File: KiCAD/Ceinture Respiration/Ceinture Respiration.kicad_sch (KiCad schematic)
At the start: 0 parts

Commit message: First draft PCB and sch
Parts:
- added A1: Arduino_Nano_v3.x, Module:Arduino_Nano, symbol MCU_Module:Arduino_Nano_v3.x
- added BT1: BH9VPC, CentureResp:BAT_BH9VPC, symbol CeintureRespAT:BH9VPC
- added C1, C2: 10uF, Capacitor_SMD:C_0603_1608Metric, symbol Device:C
- added D1, D2: DIODE, Diode_SMD:D_SOD-123, symbol pspice:DIODE
- added D3: LED, LED_THT:LED_D3.0mm, symbol Device:LED
- added D4: RED, LED_THT:LED_D3.0mm, symbol Device:LED
- added D5: ORANGE, LED_THT:LED_D3.0mm, symbol Device:LED
- added D6: GREEN, LED_THT:LED_D3.0mm, symbol Device:LED
- added D7: D_Schottky, Diode_SMD:D_SOD-123, symbol Device:D_Schottky
- added J1, J2: DIN-8, CentureResp:CUI_SDS-80J, symbol Connector:DIN-8
- added J3: Conn_01x04, Connector_PinSocket_2.54mm:PinSocket_1x04_P2.54mm_Vertical, symbol Connector_Generic:Conn_01x04
- added J4: MEM2061-01-188-00-A_REVA, CentureResp:GCT_MEM2061-01-188-00-A_REVA, symbol CeintureRespAT:MEM2061-01-188-00-A_REVA
- added J5: Conn_01x02, Buzzer_Beeper:Buzzer_Murata_PKMCS0909E, symbol Connector_Generic:Conn_01x02
- added J6: Conn_01x02, symbol Connector_Generic:Conn_01x02
- added J7: Conn_01x10_Pin, Connector_PinHeader_2.54mm:PinHeader_2x05_P2.54mm_Horizontal, symbol Connector:Conn_01x10_Pin
- added J8: Conn_01x10_Socket, Connector_PinSocket_2.54mm:PinSocket_2x05_P2.54mm_Horizontal, symbol Connector:Conn_01x10_Socket
- added PS1: RS3-0505D, CONV_RS3-0505D, symbol CeintureRespAT:RS3-0505D
- added Q1, Q2: MMBT3904, Package_TO_SOT_SMD:SOT-23, symbol Transistor_BJT:MMBT3904
- added R1, R10, R2, R3, R4, R5: 10K, Resistor_SMD:R_0603_1608Metric, symbol Device:R
- added R11, R6, R7, R8, R9: 1K, Resistor_SMD:R_0603_1608Metric, symbol Device:R
- added S1: EG1218, CentureResp:EG1218, symbol CeintureRespAT:EG1218
- added SW1, SW2, SW3, SW4: SW_Push, Button_Switch_SMD:SW_SPST_TL3305B, symbol Switch:SW_Push
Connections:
- new net: D4.2 (A), R7.1
- new net: Q2.1 (B), R2.2
- new net: Q1.1 (B), R1.2
- new net: D6.2 (A), R9.1
- new net: BT1.+, D7.2 (A)
- new net: D5.2 (A), R8.1
- new net: D7.1 (K), S1.S
- new net: J4.8 (DAT1), R5.2
- new net: J4.1 (DAT2), R4.2
- new net +3.3V: A1.17 (3V3), J3.2 (Pin_2), J4.4 (VDD), R3.1, R4.1, R5.1
- new net +5V: A1.27 (+5V), Q1.3 (C), Q2.3 (C)
- new net +5VA: J1.1, J2.1, PS1.6 (+VOUT), R6.2
- new net +BATT: J8.3 (Pin_3), PS1.2 (+VIN), S1.P
- new net -5VA: J1.4, J2.4, PS1.8 (-VOUT)
- new net A1: J7.1 (Pin_1)
- new net A2: J7.2 (Pin_2)
- new net BATT_VOLTAGE: A1.19 (A0), R10.2, R11.1
- new net BTN1: A1.25 (A6), SW2.1
- new net BTN2: A1.26 (A7), SW3.1
- new net BTN3: A1.11 (D8), SW1.1
- new net BTN4: A1.12 (D9), SW4.1
- new net BUZZER: A1.8 (D5), R1.1
- new net BUZZER_P: C1.1, D1.2 (A), J5.1 (Pin_1), Q1.2 (E)
- new net Belt_1: J1.3, J8.1 (Pin_1)
- new net Belt_2: J2.3, J8.2 (Pin_2)
- new net GND: A1.29 (GND), A1.4 (GND), C1.2, C2.2, D1.1 (K), D2.1 (K), D4.1 (K), D5.1 (K), D6.1 (K), J3.1 (Pin_1), J4.11 (GND), J4.12 (GND), J4.6 (VSS), J5.2 (Pin_2), J6.2 (Pin_2), J7.4 (Pin_4), R11.2, SW1.2, SW2.2, SW3.2, SW4.2
- new net GND1: BT1.-, D3.1 (K), J1.7, J2.7, J8.4 (Pin_4), PS1.1 (-VIN), PS1.3 (CTRL), PS1.7 (COM)
- new net LED1: A1.5 (D2), R7.2
- new net LED2: A1.6 (D3), R8.2
- new net LED3: A1.7 (D4), R9.2
- new net MISO: A1.15 (D12), J4.7 (DAT0)
- new net MOSI: A1.14 (D11), J4.3 (CMD)
- new net MOTOR: A1.9 (D6), R2.1
- new net MOTOR_P: C2.1, D2.2 (A), J6.1 (Pin_1), Q2.2 (E)
- new net PWR_LED: D3.2 (A), R6.1
- new net SCK: A1.16 (D13), J4.5 (CLK)
- new net SCL: A1.24 (A5), J3.3 (Pin_3)
- new net SDA: A1.23 (A4), J3.4 (Pin_4)
- new net SD_CS: A1.13 (D10), J4.2 (CD/DAT3), R3.2
- new net Signal_1: A1.20 (A1)
- new net Signal_2: A1.21 (A2)
- new net VDD: A1.30 (VIN), J7.3 (Pin_3), R10.1
- no-connect marks 0 -> 2
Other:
- removed sheet CONNECTOR
- removed sheet DEVICES
- removed sheet MCU
- removed sheet PSU
- note added: "BUZZER"
- note added: "DIN 8P -> SDS-80J"
- note added: "GOGOSSE Switch-1/0 2X BTN Vibration Buzzer LED PWR LED Indicator RGB SD card"
- note added: "I2C Screen"
- note added: "INPUT RANGE 4.5V-9V"
- note added: "MCU NANO PINOUT ARDUINO NANO BLE 33"
- note added: "RS3-0505D avec une batterie 9V"
- note added: "Référence https://content.arduino.cc/assets/NANO33BLE_V4.0_sch.pdf?_gl=1*1v2d5tn*_ga*MTgwOTc4MjI5MC4xNjg2OTY2OTQz*_ga_NEXN8H46L5*MTY4Njk3MDgyNi4yLjEuMTY4Njk3MTE2NC4wLjAuMA.."
- note added: "VIB"
- note added: "connector for sensor DIN"
- note removed: "AUTRE GOGOSSE Switch-1/0 2X BTN Vibration Buzzer LED PWR LED Indicator RGB SD card"
- note removed: "Connector USB-C - programming connector for sensor DIN JST PH li-po"
- note removed: "MCU Feather datalogger ..."
- note removed: "PSU +/- 12V Li-Po USB Charge"

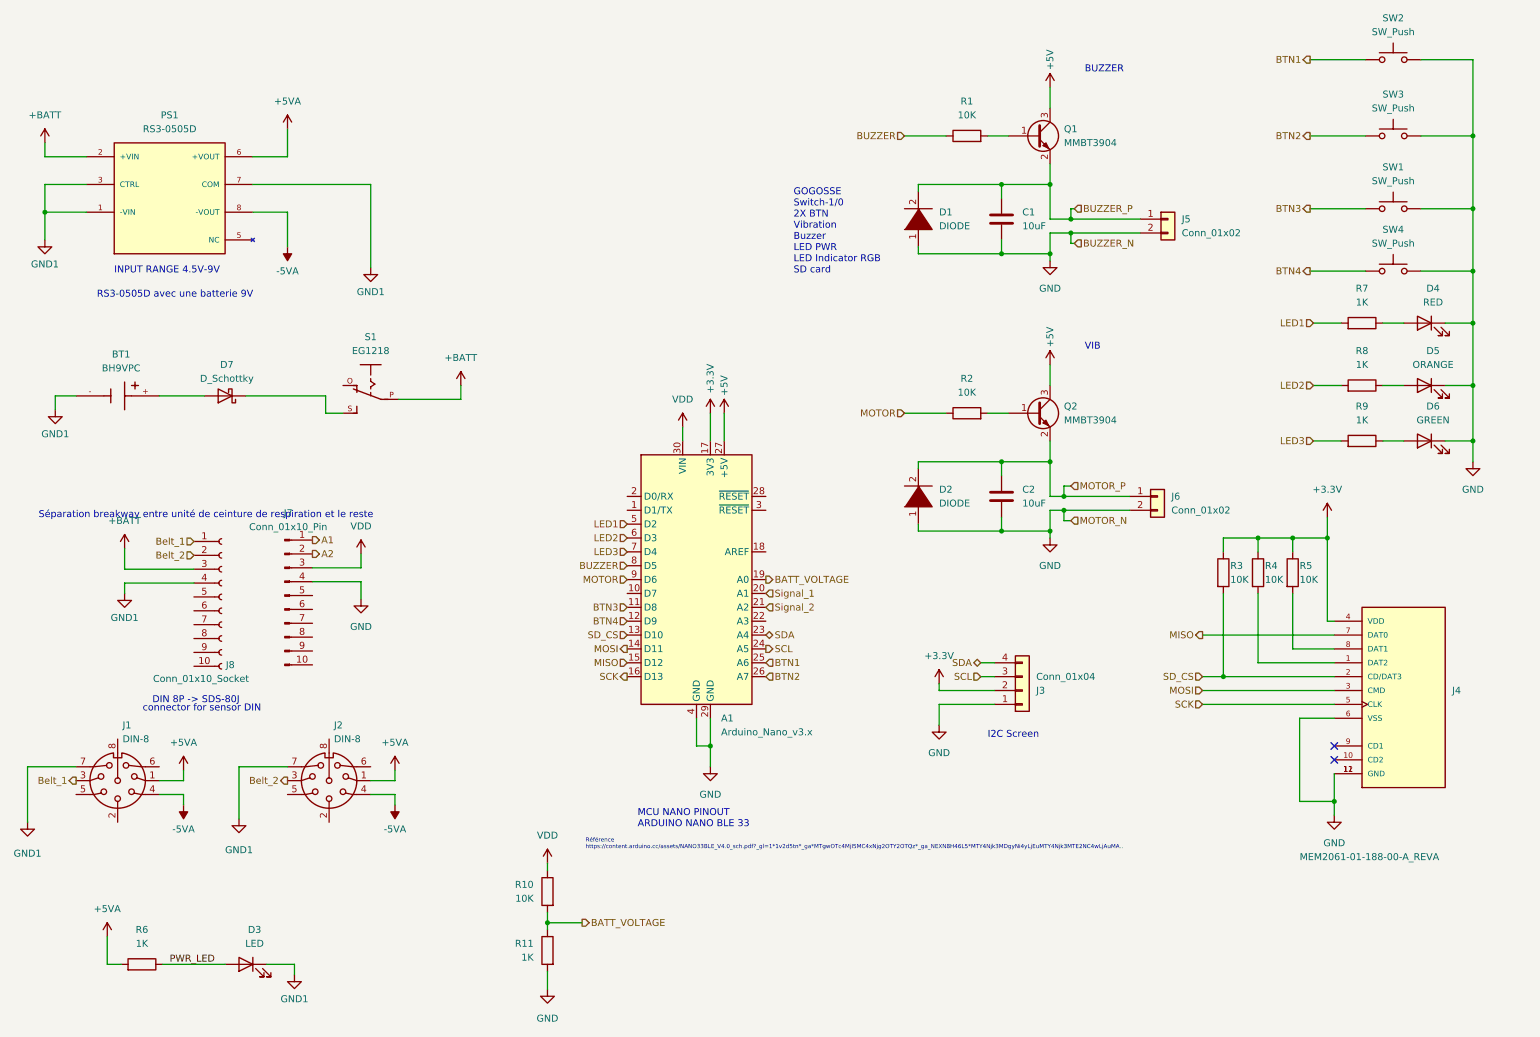
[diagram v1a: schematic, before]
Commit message: Scématique complété
Reste quelques footprint à configurer
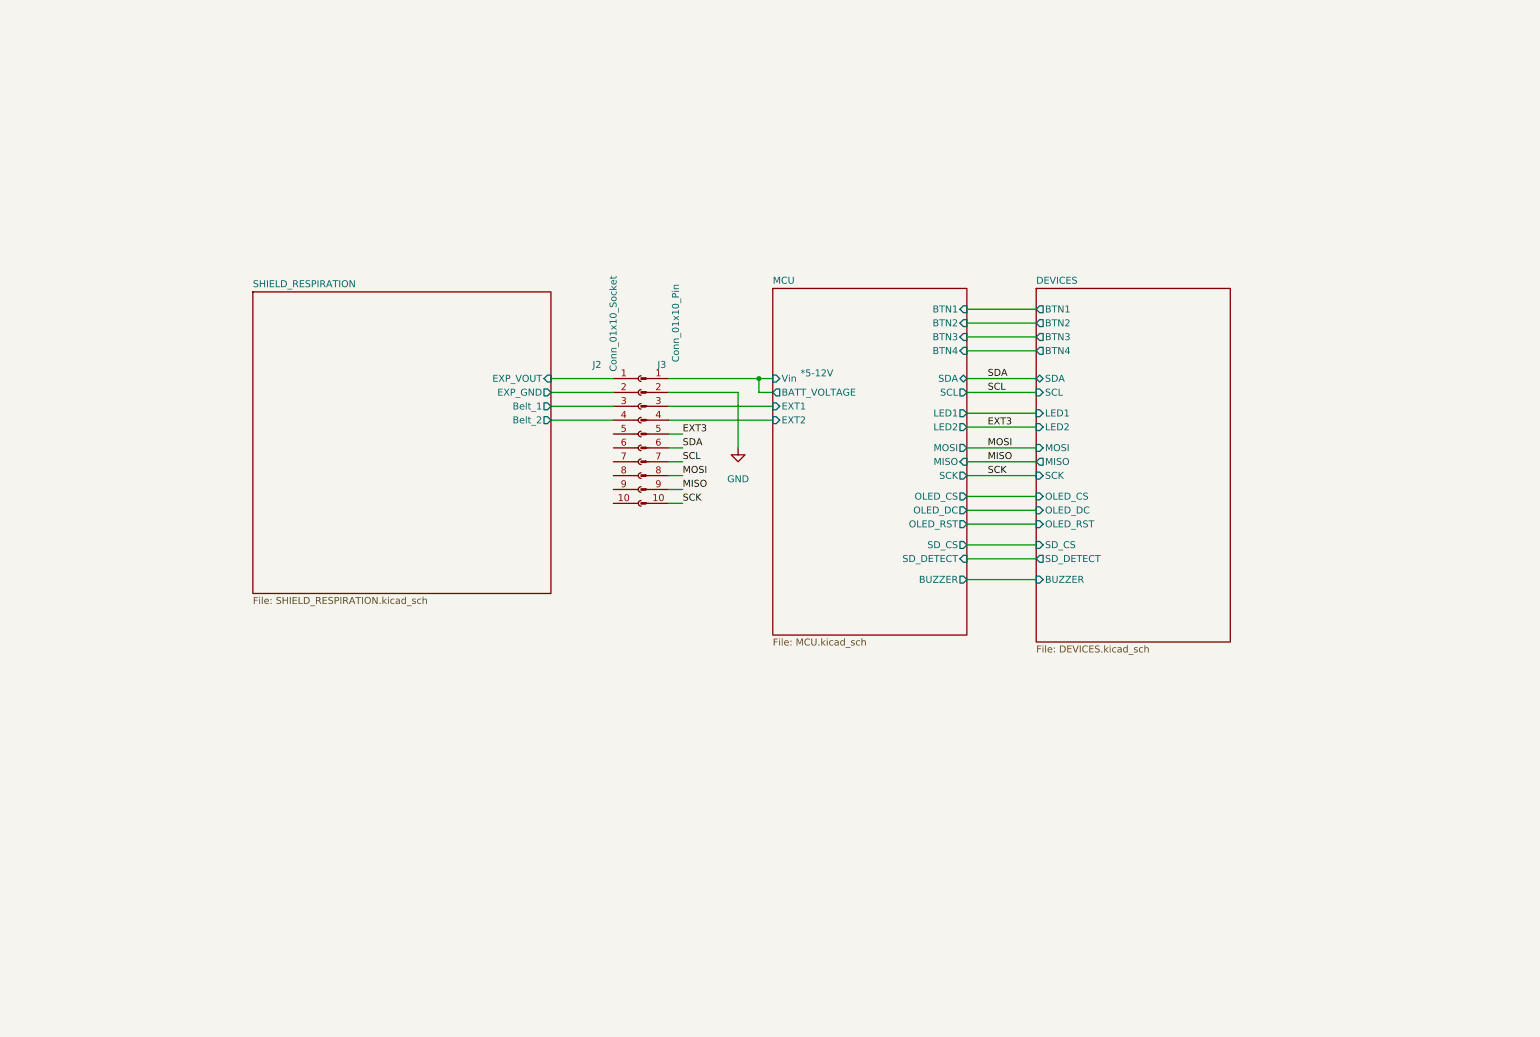
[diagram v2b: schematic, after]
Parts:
- removed A1: Arduino_Nano_v3.x, Module:Arduino_Nano, symbol MCU_Module:Arduino_Nano_v3.x
- removed BT1: BH9VPC, CentureResp:BAT_BH9VPC, symbol CeintureRespAT:BH9VPC
- removed C1, C2: 10uF, Capacitor_SMD:C_0603_1608Metric, symbol Device:C
- removed D1, D2: DIODE, Diode_SMD:D_SOD-123, symbol pspice:DIODE
- removed D3: LED, LED_THT:LED_D3.0mm, symbol Device:LED
- removed D4: RED, LED_THT:LED_D3.0mm, symbol Device:LED
- removed D5: ORANGE, LED_THT:LED_D3.0mm, symbol Device:LED
- removed D6: GREEN, LED_THT:LED_D3.0mm, symbol Device:LED
- removed D7: D_Schottky, Diode_SMD:D_SOD-123, symbol Device:D_Schottky
- removed J1, J2: DIN-8, CentureResp:CUI_SDS-80J, symbol Connector:DIN-8
- removed J3: Conn_01x04, Connector_PinSocket_2.54mm:PinSocket_1x04_P2.54mm_Vertical, symbol Connector_Generic:Conn_01x04
- removed J4: MEM2061-01-188-00-A_REVA, CentureResp:GCT_MEM2061-01-188-00-A_REVA, symbol CeintureRespAT:MEM2061-01-188-00-A_REVA
- removed J5: Conn_01x02, Buzzer_Beeper:Buzzer_Murata_PKMCS0909E, symbol Connector_Generic:Conn_01x02
- removed J6: Conn_01x02, symbol Connector_Generic:Conn_01x02
- removed J7: Conn_01x10_Pin, Connector_PinHeader_2.54mm:PinHeader_2x05_P2.54mm_Horizontal, symbol Connector:Conn_01x10_Pin
- removed J8: Conn_01x10_Socket, Connector_PinSocket_2.54mm:PinSocket_2x05_P2.54mm_Horizontal, symbol Connector:Conn_01x10_Socket
- removed PS1: RS3-0505D, CONV_RS3-0505D, symbol CeintureRespAT:RS3-0505D
- removed Q1, Q2: MMBT3904, Package_TO_SOT_SMD:SOT-23, symbol Transistor_BJT:MMBT3904
- removed R1, R10, R2, R3, R4, R5: 10K, Resistor_SMD:R_0603_1608Metric, symbol Device:R
- removed R11, R6, R7, R8, R9: 1K, Resistor_SMD:R_0603_1608Metric, symbol Device:R
- removed S1: EG1218, CentureResp:EG1218, symbol CeintureRespAT:EG1218
- removed SW1, SW2, SW3, SW4: SW_Push, Button_Switch_SMD:SW_SPST_TL3305B, symbol Switch:SW_Push
- added J2: Conn_01x10_Socket, Connector_PinSocket_2.54mm:PinSocket_2x05_P2.54mm_Horizontal, symbol Connector:Conn_01x10_Socket
- added J3: Conn_01x10_Pin, Connector_PinHeader_2.54mm:PinHeader_2x05_P2.54mm_Horizontal, symbol Connector:Conn_01x10_Pin
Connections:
- net GND: now also J3.2 (Pin_2)
- net MISO: now also J3.9 (Pin_9)
- net MOSI: now also J3.8 (Pin_8)
- net SCK: now also J3.10 (Pin_10)
- net SCL: now also J3.7 (Pin_7)
- net SDA: now also J3.6 (Pin_6)
- new net EXT3: J3.5 (Pin_5)
- new net MCU/BATT_VOLTAGE: J3.1 (Pin_1)
- new net MCU/EXT1: J3.3 (Pin_3)
- new net MCU/EXT2: J3.4 (Pin_4)
- new net SHIELD_RESPIRATION/Belt_1: J2.3 (Pin_3)
- new net SHIELD_RESPIRATION/Belt_2: J2.4 (Pin_4)
- new net SHIELD_RESPIRATION/EXP_GND: J2.2 (Pin_2)
- new net SHIELD_RESPIRATION/EXP_VOUT: J2.1 (Pin_1)
- no-connect marks 2 -> 0
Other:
- added sheet DEVICES (DEVICES.kicad_sch)
- added sheet MCU (MCU.kicad_sch)
- added sheet SHIELD_RESPIRATION (SHIELD_RESPIRATION.kicad_sch)
- note added: "*5-12V"
- note removed: "BUZZER"
- note removed: "DIN 8P -> SDS-80J"
- note removed: "GOGOSSE Switch-1/0 2X BTN Vibration Buzzer LED PWR LED Indicator RGB SD card"
- note removed: "I2C Screen"
- note removed: "INPUT RANGE 4.5V-9V"
- note removed: "MCU NANO PINOUT ARDUINO NANO BLE 33"
- note removed: "RS3-0505D avec une batterie 9V"
- note removed: "Référence https://content.arduino.cc/assets/NANO33BLE_V4.0_sch.pdf?_gl=1*1v2d5tn*_ga*MTgwOTc4MjI5MC4xNjg2OTY2OTQz*_ga_NEXN8H46L5*MTY4Njk3MDgyNi4yLjEuMTY4Njk3MTE2NC4wLjAuMA.."
- note removed: "Séparation breakway entre unité de ceinture de respiration et le reste"
- note removed: "VIB"
- note removed: "connector for sensor DIN"
- title: (none) -> Plateforme Portable AT

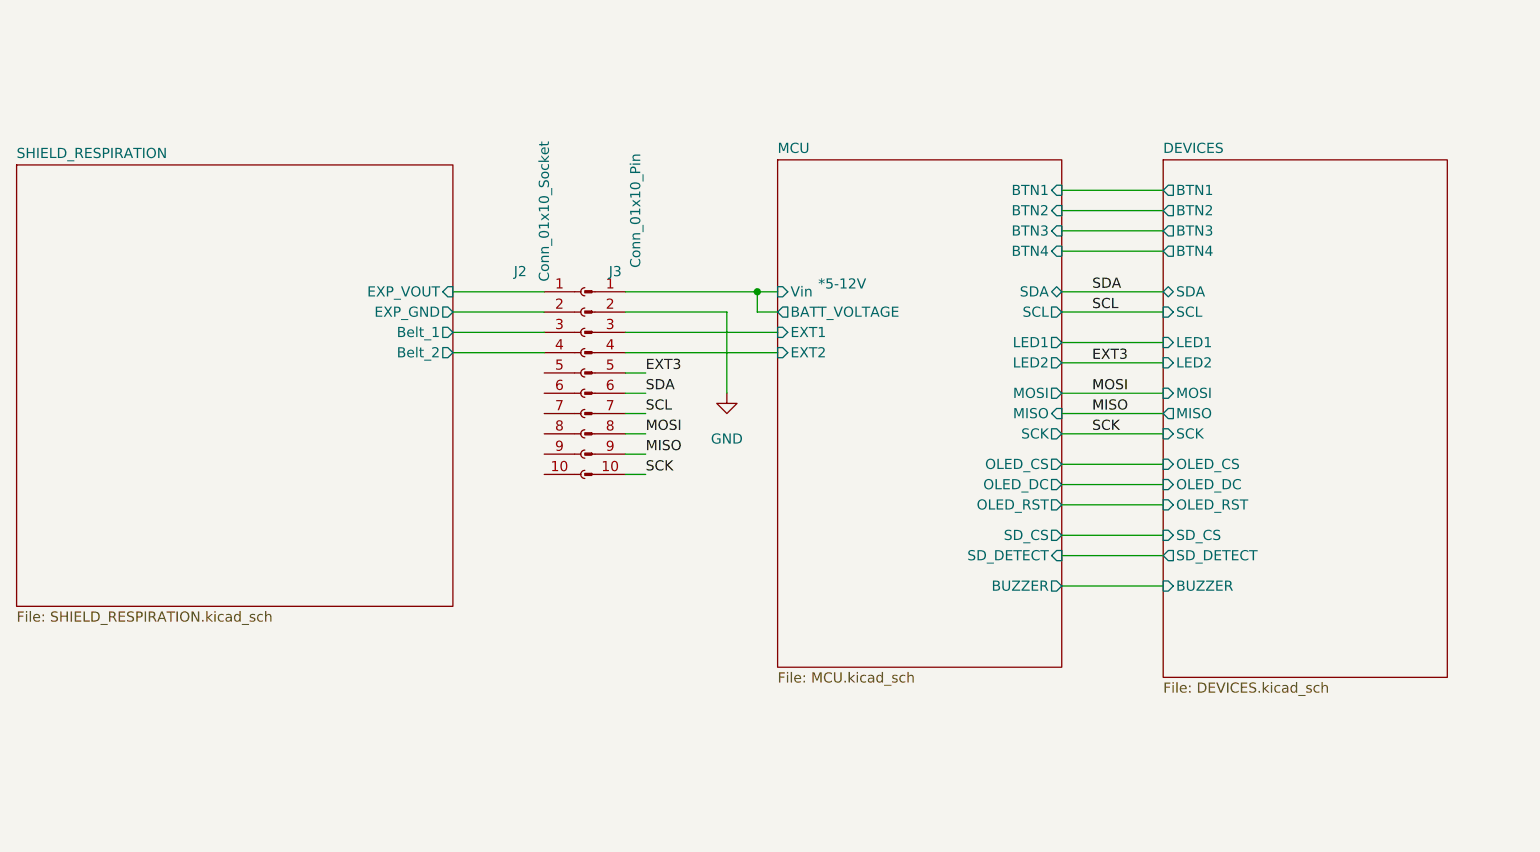
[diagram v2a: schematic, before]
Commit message: Schematique 99%, PCB 50%
schématique complété, nettoyé et layout complété, reste routage
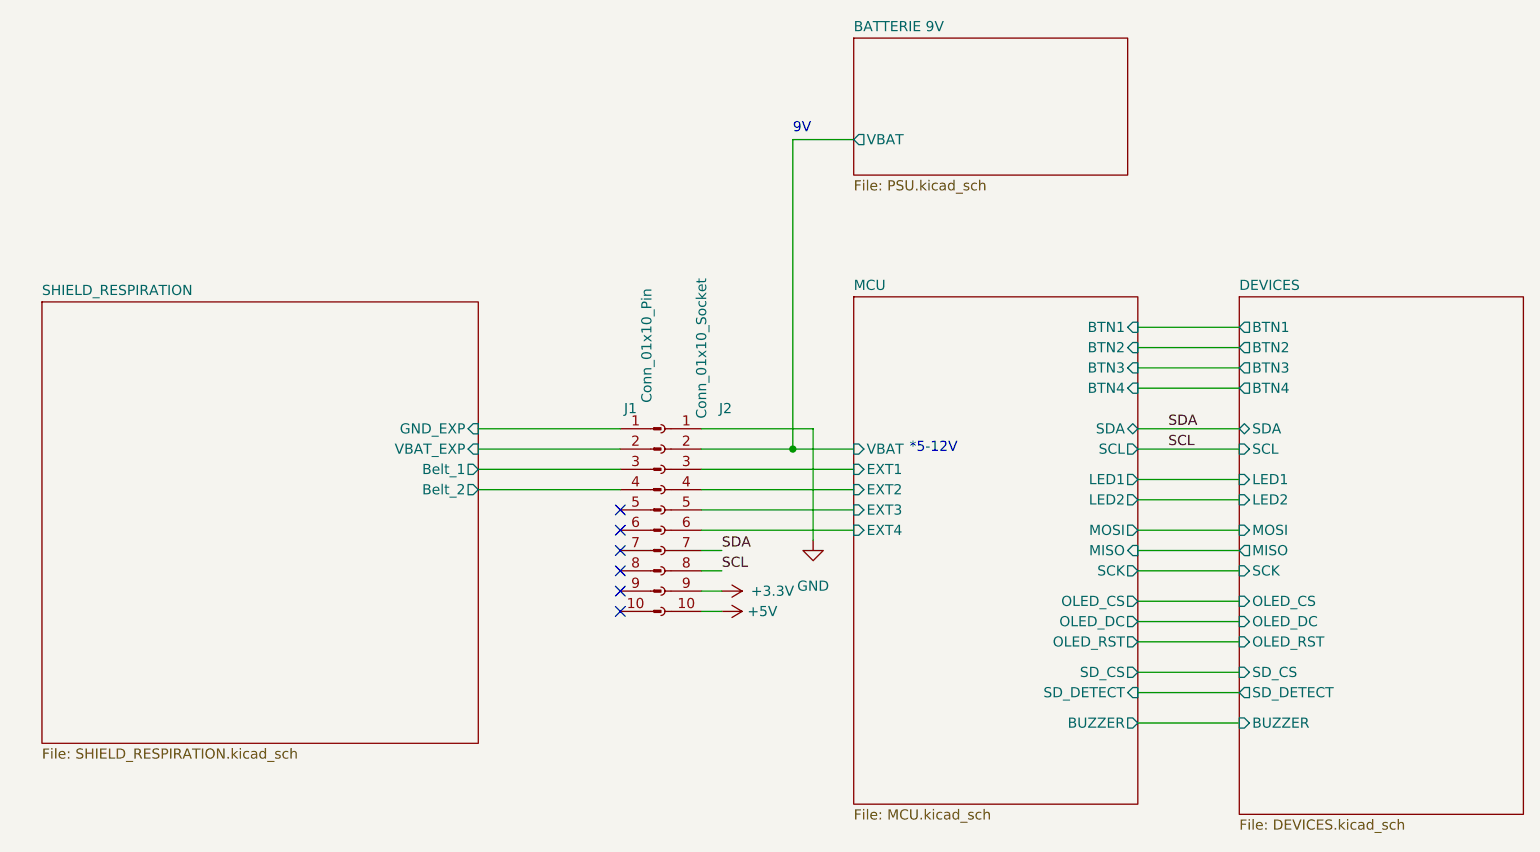
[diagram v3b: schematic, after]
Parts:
- J1: renamed from J3; footprint Connector_PinHeader_2.54mm:PinHeader_2x05_P2.54mm_Horizontal -> Connector_PinHeader_2.54mm:PinHeader_1x10_P2.54mm_Vertical
- J2: footprint Connector_PinSocket_2.54mm:PinSocket_2x05_P2.54mm_Horizontal -> Connector_PinSocket_2.54mm:PinSocket_1x10_P2.54mm_Vertical
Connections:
- net SHIELD_RESPIRATION/EXP_VOUT is gone; now on net GND: J2.1 (Pin_1)
- net GND: no longer J1.2 (Pin_2)
- net MCU/EXT1: now also J2.3 (Pin_3); no longer J1.3 (Pin_3)
- net MCU/EXT2: now also J2.4 (Pin_4); no longer J1.4 (Pin_4)
- net SCL: now also J2.8 (Pin_8); no longer J1.7 (Pin_7)
- net SDA: now also J2.7 (Pin_7); no longer J1.6 (Pin_6)
- net SHIELD_RESPIRATION/Belt_1: now also J1.3 (Pin_3); no longer J2.3 (Pin_3)
- net SHIELD_RESPIRATION/Belt_2: now also J1.4 (Pin_4); no longer J2.4 (Pin_4)
- net +5V: now reaches J2.10 (Pin_10)
- net MCU/EXT3: now reaches J2.5 (Pin_5)
- net MCU/EXT4: now reaches J2.6 (Pin_6)
- net +3.3V: now reaches J2.9 (Pin_9)
- net EXT3: no longer names the net of J1.5 (Pin_5)
- net MCU/BATT_VOLTAGE renamed SHIELD_RESPIRATION/GND_EXP
- net MISO: no longer names the net of J1.9 (Pin_9)
- net MOSI: no longer names the net of J1.8 (Pin_8)
- net SCK: no longer names the net of J1.10 (Pin_10)
- net SHIELD_RESPIRATION/EXP_GND renamed BATTERIE 9V/VBAT
- new net SHIELD_RESPIRATION/VBAT_EXP: J1.2 (Pin_2)
- no-connect marks 0 -> 6
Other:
- added sheet BATTERIE 9V (PSU.kicad_sch)
- sheet MCU ports: added EXT3, EXT4, VBAT; removed BATT_VOLTAGE, Vin
- sheet SHIELD_RESPIRATION ports: added GND_EXP, VBAT_EXP; removed EXP_GND, EXP_VOUT
- note added: "9V"
- company: (none) -> IngRéadapt UL
- moved on the sheet: J1, J2

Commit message: sch 99% pcb 99%
Reste à préparer les commandes
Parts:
- added F1, F2, F3: 500mA, Fuse:Fuse_0603_1608Metric, symbol Device:Polyfuse
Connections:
- net +3.3V: now also F1.2; no longer J2.9 (Pin_9)
- net +5V: now also F2.2; no longer J2.10 (Pin_10)
- net BATTERIE 9V/VBAT: now also F3.2; no longer J2.2 (Pin_2)
- new net: F2.1, J2.10 (Pin_10)
- new net: F3.1, J2.2 (Pin_2)
- new net: F1.1, J2.9 (Pin_9)
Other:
- moved on the sheet: J1, J2
